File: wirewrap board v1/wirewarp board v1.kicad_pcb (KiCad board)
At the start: 2 copper layers, 99.1 x 99.1 mm, 1369 parts

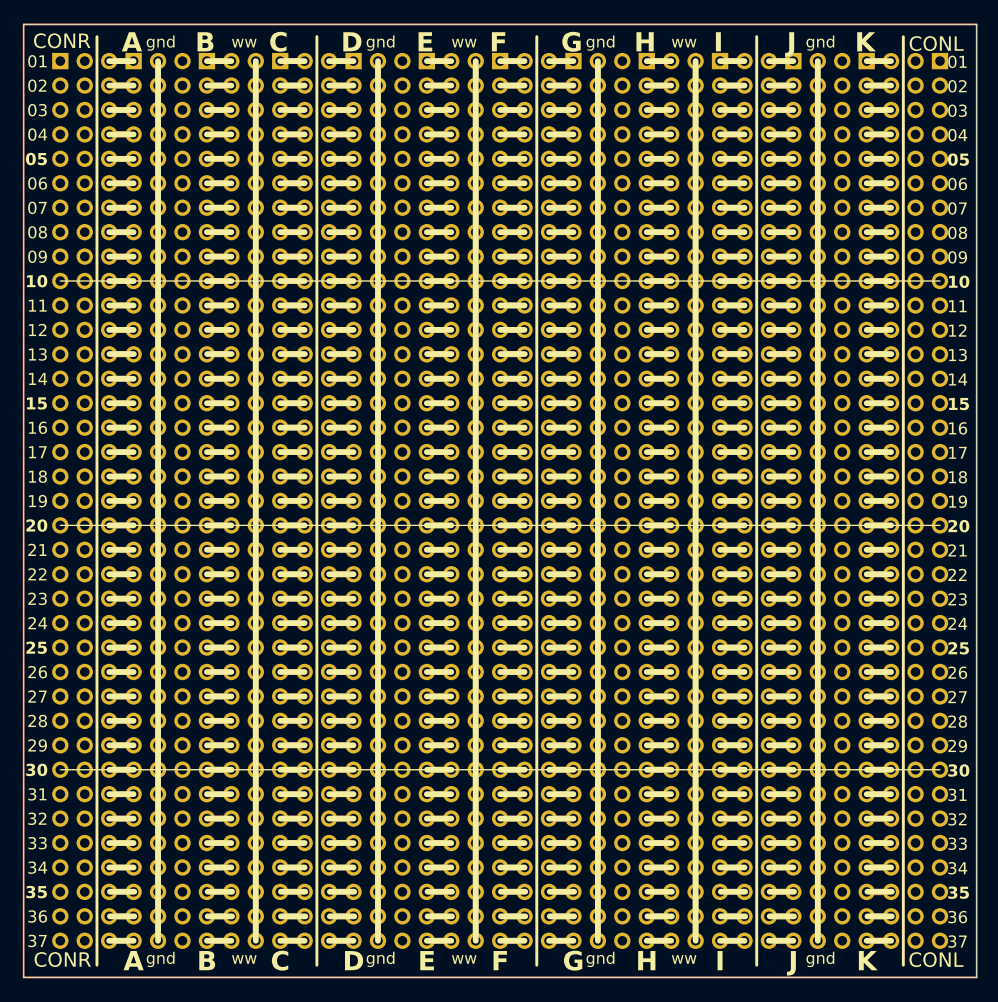
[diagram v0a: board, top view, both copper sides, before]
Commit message: protoboard for wire wrap kicad added v1 v2
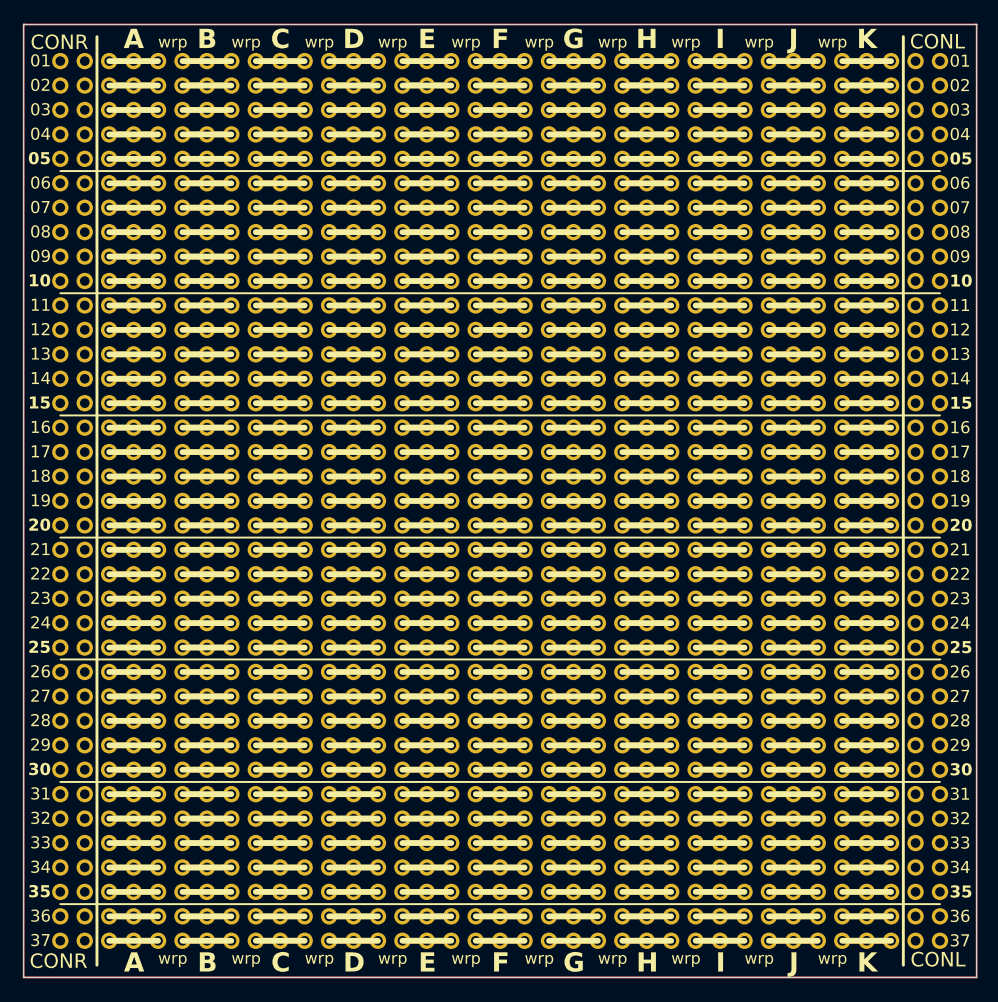
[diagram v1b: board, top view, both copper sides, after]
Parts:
- removed ? (x1369): , 
- added 100: , , F.Cu at (146.1, 82.5)
- added 1000: , , F.Cu at (115.6, 146.1)
- added 1001: , , F.Cu at (115.6, 143.5)
- added 1002: , , F.Cu at (115.6, 141.0)
- added 1003: , , F.Cu at (115.6, 138.4)
- added 1004: , , F.Cu at (115.6, 135.9)
- added 1005: , , F.Cu at (115.6, 133.3)
- added 1006: , , F.Cu at (115.6, 130.8)
- added 1007: , , F.Cu at (115.6, 128.3)
- added 1008: , , F.Cu at (115.6, 125.7)
- added 1009: , , F.Cu at (115.6, 123.2)
- added 101: , , F.Cu at (146.1, 80.0)
- added 1010: , , F.Cu at (115.6, 120.7)
- added 1011: , , F.Cu at (115.6, 118.1)
- added 1012: , , F.Cu at (115.6, 115.6)
- added 1013: , , F.Cu at (115.6, 113.0)
- added 1014: , , F.Cu at (115.6, 110.5)
- added 1015: , , F.Cu at (115.6, 108.0)
- added 1016: , , F.Cu at (115.6, 105.4)
- added 1017: , , F.Cu at (115.6, 102.9)
- added 1018: , , F.Cu at (115.6, 100.3)
- added 1019: , , F.Cu at (115.6, 97.8)
- added 102: , , F.Cu at (146.1, 77.5)
- added 1020: , , F.Cu at (115.6, 95.2)
- added 1021: , , F.Cu at (115.6, 92.7)
- added 1022: , , F.Cu at (115.6, 90.2)
- added 1023: , , F.Cu at (115.6, 87.6)
- added 1024: , , F.Cu at (115.6, 85.1)
- added 1025: , , F.Cu at (115.6, 82.5)
- added 1026: , , F.Cu at (115.6, 80.0)
- added 1027: , , F.Cu at (115.6, 77.5)
- added 1028: , , F.Cu at (115.6, 74.9)
- added 1029: , , F.Cu at (115.6, 72.4)
- added 103: , , F.Cu at (146.1, 74.9)
- added 1030: , , F.Cu at (115.6, 69.8)
- added 1031: , , F.Cu at (115.6, 67.3)
- added 1032: , , F.Cu at (115.6, 64.8)
- added 1033: , , F.Cu at (115.6, 62.2)
- added 1034: , , F.Cu at (115.6, 59.7)
- added 1035: , , F.Cu at (115.6, 57.1)
- added 1036: , , F.Cu at (115.6, 54.6)
- added 1037: , , F.Cu at (118.1, 146.1)
- added 1038: , , F.Cu at (118.1, 143.5)
- added 1039: , , F.Cu at (118.1, 141.0)
- added 104: , , F.Cu at (146.1, 72.4)
- added 1040: , , F.Cu at (118.1, 138.4)
- added 1041: , , F.Cu at (118.1, 135.9)
- added 1042: , , F.Cu at (118.1, 133.3)
- added 1043: , , F.Cu at (118.1, 130.8)
- added 1044: , , F.Cu at (118.1, 128.3)
- added 1045: , , F.Cu at (118.1, 125.7)
- added 1046: , , F.Cu at (118.1, 123.2)
- added 1047: , , F.Cu at (118.1, 120.7)
- added 1048: , , F.Cu at (118.1, 118.1)
- added 1049: , , F.Cu at (118.1, 115.6)
- added 105: , , F.Cu at (146.1, 69.8)
- added 1050: , , F.Cu at (118.1, 113.0)
- added 1051: , , F.Cu at (118.1, 110.5)
- added 1052: , , F.Cu at (118.1, 108.0)
- added 1053: , , F.Cu at (118.1, 105.4)
- added 1054: , , F.Cu at (118.1, 102.9)
- added 1055: , , F.Cu at (118.1, 100.3)
- added 1056: , , F.Cu at (118.1, 97.8)
- added 1057: , , F.Cu at (118.1, 95.2)
- added 1058: , , F.Cu at (118.1, 92.7)
- added 1059: , , F.Cu at (118.1, 90.2)
- added 106: , , F.Cu at (146.1, 67.3)
- added 1060: , , F.Cu at (118.1, 87.6)
- added 1061: , , F.Cu at (118.1, 85.1)
- added 1062: , , F.Cu at (118.1, 82.5)
- added 1063: , , F.Cu at (118.1, 80.0)
- added 1064: , , F.Cu at (118.1, 77.5)
- added 1065: , , F.Cu at (118.1, 74.9)
- added 1066: , , F.Cu at (118.1, 72.4)
- added 1067: , , F.Cu at (118.1, 69.8)
- added 1068: , , F.Cu at (118.1, 67.3)
- added 1069: , , F.Cu at (118.1, 64.8)
- added 107: , , F.Cu at (146.1, 64.8)
- added 1070: , , F.Cu at (118.1, 62.2)
- added 1071: , , F.Cu at (118.1, 59.7)
- added 1072: , , F.Cu at (118.1, 57.1)
- added 1073: , , F.Cu at (118.1, 54.6)
- added 1074: , , F.Cu at (120.7, 146.1)
- added 1075: , , F.Cu at (120.7, 143.5)
- added 1076: , , F.Cu at (120.7, 141.0)
- added 1077: , , F.Cu at (120.7, 138.4)
- added 1078: , , F.Cu at (120.7, 135.9)
- added 1079: , , F.Cu at (120.7, 133.3)
- added 108: , , F.Cu at (146.1, 62.2)
- added 1080: , , F.Cu at (120.7, 130.8)
- added 1081: , , F.Cu at (120.7, 128.3)
- added 1082: , , F.Cu at (120.7, 125.7)
- added 1083: , , F.Cu at (120.7, 123.2)
- added 1084: , , F.Cu at (120.7, 120.7)
- added 1085: , , F.Cu at (120.7, 118.1)
- added 1086: , , F.Cu at (120.7, 115.6)
- added 1087: , , F.Cu at (120.7, 113.0)
- added 1088: , , F.Cu at (120.7, 110.5)
- added 1089: , , F.Cu at (120.7, 108.0)
- added 109: , , F.Cu at (146.1, 59.7)
- added 1090: , , F.Cu at (120.7, 105.4)
- added 1091: , , F.Cu at (120.7, 102.9)
- added 1092: , , F.Cu at (120.7, 100.3)
- added 1093: , , F.Cu at (120.7, 97.8)
- added 1094: , , F.Cu at (120.7, 95.2)
- added 1095: , , F.Cu at (120.7, 92.7)
- added 1096: , , F.Cu at (120.7, 90.2)
- added 1097: , , F.Cu at (120.7, 87.6)
- added 1098: , , F.Cu at (120.7, 85.1)
- added 1099: , , F.Cu at (120.7, 82.5)
- added 110: , , F.Cu at (146.1, 57.1)
- added 1100: , , F.Cu at (120.7, 80.0)
- added 1101: , , F.Cu at (120.7, 77.5)
- added 1102: , , F.Cu at (120.7, 74.9)
- added 1103: , , F.Cu at (120.7, 72.4)
- added 1104: , , F.Cu at (120.7, 69.8)
- added 1105: , , F.Cu at (120.7, 67.3)
- added 1106: , , F.Cu at (120.7, 64.8)
- added 1107: , , F.Cu at (120.7, 62.2)
- added 1108: , , F.Cu at (120.7, 59.7)
- added 1109: , , F.Cu at (120.7, 57.1)
- added 111: , , F.Cu at (146.1, 54.6)
- added 1110: , , F.Cu at (120.7, 54.6)
- added 1111: , , F.Cu at (123.2, 146.1)
- added 1112: , , F.Cu at (123.2, 143.5)
- added 1113: , , F.Cu at (123.2, 141.0)
- added 1114: , , F.Cu at (123.2, 138.4)
- added 1115: , , F.Cu at (123.2, 135.9)
- added 1116: , , F.Cu at (123.2, 133.3)
- added 1117: , , F.Cu at (123.2, 130.8)
- added 1118: , , F.Cu at (123.2, 128.3)
- added 1119: , , F.Cu at (123.2, 125.7)
- added 112: , , F.Cu at (54.6, 146.1)
- added 1120: , , F.Cu at (123.2, 123.2)
- added 1121: , , F.Cu at (123.2, 120.7)
- added 1122: , , F.Cu at (123.2, 118.1)
- added 1123: , , F.Cu at (123.2, 115.6)
- added 1124: , , F.Cu at (123.2, 113.0)
- added 1125: , , F.Cu at (123.2, 110.5)
- added 1126: , , F.Cu at (123.2, 108.0)
- added 1127: , , F.Cu at (123.2, 105.4)
- added 1128: , , F.Cu at (123.2, 102.9)
- added 1129: , , F.Cu at (123.2, 100.3)
- added 113: , , F.Cu at (54.6, 143.5)
- added 1130: , , F.Cu at (123.2, 97.8)
- added 1131: , , F.Cu at (123.2, 95.2)
- added 1132: , , F.Cu at (123.2, 92.7)
- added 1133: , , F.Cu at (123.2, 90.2)
- added 1134: , , F.Cu at (123.2, 87.6)
- added 1135: , , F.Cu at (123.2, 85.1)
- added 1136: , , F.Cu at (123.2, 82.5)
- added 1137: , , F.Cu at (123.2, 80.0)
- added 1138: , , F.Cu at (123.2, 77.5)
- added 1139: , , F.Cu at (123.2, 74.9)
- added 114: , , F.Cu at (54.6, 141.0)
- added 1140: , , F.Cu at (123.2, 72.4)
- added 1141: , , F.Cu at (123.2, 69.8)
- added 1142: , , F.Cu at (123.2, 67.3)
- added 1143: , , F.Cu at (123.2, 64.8)
- added 1144: , , F.Cu at (123.2, 62.2)
- added 1145: , , F.Cu at (123.2, 59.7)
- added 1146: , , F.Cu at (123.2, 57.1)
- added 1147: , , F.Cu at (123.2, 54.6)
- added 1148: , , F.Cu at (125.7, 146.1)
- added 1149: , , F.Cu at (125.7, 143.5)
- added 115: , , F.Cu at (54.6, 138.4)
- added 1150: , , F.Cu at (125.7, 141.0)
- added 1151: , , F.Cu at (125.7, 138.4)
- added 1152: , , F.Cu at (125.7, 135.9)
- added 1153: , , F.Cu at (125.7, 133.3)
- added 1154: , , F.Cu at (125.7, 130.8)
- added 1155: , , F.Cu at (125.7, 128.3)
- added 1156: , , F.Cu at (125.7, 125.7)
- added 1157: , , F.Cu at (125.7, 123.2)
- added 1158: , , F.Cu at (125.7, 120.7)
- added 1159: , , F.Cu at (125.7, 118.1)
- added 116: , , F.Cu at (54.6, 135.9)
- added 1160: , , F.Cu at (125.7, 115.6)
- added 1161: , , F.Cu at (125.7, 113.0)
- added 1162: , , F.Cu at (125.7, 110.5)
- added 1163: , , F.Cu at (125.7, 108.0)
- added 1164: , , F.Cu at (125.7, 105.4)
- added 1165: , , F.Cu at (125.7, 102.9)
- added 1166: , , F.Cu at (125.7, 100.3)
- added 1167: , , F.Cu at (125.7, 97.8)
- added 1168: , , F.Cu at (125.7, 95.2)
- added 1169: , , F.Cu at (125.7, 92.7)
- added 117: , , F.Cu at (54.6, 133.3)
- added 1170: , , F.Cu at (125.7, 90.2)
- added 1171: , , F.Cu at (125.7, 87.6)
- added 1172: , , F.Cu at (125.7, 85.1)
- added 1173: , , F.Cu at (125.7, 82.5)
- added 1174: , , F.Cu at (125.7, 80.0)
- added 1175: , , F.Cu at (125.7, 77.5)
- added 1176: , , F.Cu at (125.7, 74.9)
- added 1177: , , F.Cu at (125.7, 72.4)
- added 1178: , , F.Cu at (125.7, 69.8)
- added 1179: , , F.Cu at (125.7, 67.3)
- added 118: , , F.Cu at (54.6, 130.8)
- added 1180: , , F.Cu at (125.7, 64.8)
- added 1181: , , F.Cu at (125.7, 62.2)
- added 1182: , , F.Cu at (125.7, 59.7)
- added 1183: , , F.Cu at (125.7, 57.1)
- added 1184: , , F.Cu at (125.7, 54.6)
- added 1185: , , F.Cu at (128.3, 146.1)
- added 1186: , , F.Cu at (128.3, 143.5)
- added 1187: , , F.Cu at (128.3, 141.0)
- added 1188: , , F.Cu at (128.3, 138.4)
- added 1189: , , F.Cu at (128.3, 135.9)
- added 119: , , F.Cu at (54.6, 128.3)
- added 1190: , , F.Cu at (128.3, 133.3)
- added 1191: , , F.Cu at (128.3, 130.8)
- added 1192: , , F.Cu at (128.3, 128.3)
- added 1193: , , F.Cu at (128.3, 125.7)
- added 1194: , , F.Cu at (128.3, 123.2)
- added 1195: , , F.Cu at (128.3, 120.7)
- added 1196: , , F.Cu at (128.3, 118.1)
- added 1197: , , F.Cu at (128.3, 115.6)
- added 1198: , , F.Cu at (128.3, 113.0)
- added 1199: , , F.Cu at (128.3, 110.5)
- added 120: , , F.Cu at (54.6, 125.7)
- added 1200: , , F.Cu at (128.3, 108.0)
- added 1201: , , F.Cu at (128.3, 105.4)
- added 1202: , , F.Cu at (128.3, 102.9)
- added 1203: , , F.Cu at (128.3, 100.3)
- added 1204: , , F.Cu at (128.3, 97.8)
- added 1205: , , F.Cu at (128.3, 95.2)
- added 1206: , , F.Cu at (128.3, 92.7)
- added 1207: , , F.Cu at (128.3, 90.2)
- added 1208: , , F.Cu at (128.3, 87.6)
- added 1209: , , F.Cu at (128.3, 85.1)
- added 121: , , F.Cu at (54.6, 123.2)
- added 1210: , , F.Cu at (128.3, 82.5)
- added 1211: , , F.Cu at (128.3, 80.0)
- added 1212: , , F.Cu at (128.3, 77.5)
- added 1213: , , F.Cu at (128.3, 74.9)
- added 1214: , , F.Cu at (128.3, 72.4)
- added 1215: , , F.Cu at (128.3, 69.8)
- added 1216: , , F.Cu at (128.3, 67.3)
- added 1217: , , F.Cu at (128.3, 64.8)
- added 1218: , , F.Cu at (128.3, 62.2)
- added 1219: , , F.Cu at (128.3, 59.7)
- added 122: , , F.Cu at (54.6, 120.7)
- added 1220: , , F.Cu at (128.3, 57.1)
- added 1221: , , F.Cu at (128.3, 54.6)
- added 1222: , , F.Cu at (130.8, 146.1)
- added 1223: , , F.Cu at (130.8, 143.5)
- added 1224: , , F.Cu at (130.8, 141.0)
- added 1225: , , F.Cu at (130.8, 138.4)
- added 1226: , , F.Cu at (130.8, 135.9)
- added 1227: , , F.Cu at (130.8, 133.3)
- added 1228: , , F.Cu at (130.8, 130.8)
- added 1229: , , F.Cu at (130.8, 128.3)
- added 123: , , F.Cu at (54.6, 118.1)
- added 1230: , , F.Cu at (130.8, 125.7)
- added 1231: , , F.Cu at (130.8, 123.2)
- added 1232: , , F.Cu at (130.8, 120.7)
- added 1233: , , F.Cu at (130.8, 118.1)
- added 1234: , , F.Cu at (130.8, 115.6)
- added 1235: , , F.Cu at (130.8, 113.0)
- added 1236: , , F.Cu at (130.8, 110.5)
- added 1237: , , F.Cu at (130.8, 108.0)
- added 1238: , , F.Cu at (130.8, 105.4)
- added 1239: , , F.Cu at (130.8, 102.9)
- added 124: , , F.Cu at (54.6, 115.6)
- added 1240: , , F.Cu at (130.8, 100.3)
- added 1241: , , F.Cu at (130.8, 97.8)
- added 1242: , , F.Cu at (130.8, 95.2)
- added 1243: , , F.Cu at (130.8, 92.7)
- added 1244: , , F.Cu at (130.8, 90.2)
- added 1245: , , F.Cu at (130.8, 87.6)
- added 1246: , , F.Cu at (130.8, 85.1)
- added 1247: , , F.Cu at (130.8, 82.5)
- added 1248: , , F.Cu at (130.8, 80.0)
- added 1249: , , F.Cu at (130.8, 77.5)
- added 125: , , F.Cu at (54.6, 113.0)
- added 1250: , , F.Cu at (130.8, 74.9)
- added 1251: , , F.Cu at (130.8, 72.4)
- added 1252: , , F.Cu at (130.8, 69.8)
- added 1253: , , F.Cu at (130.8, 67.3)
- added 1254: , , F.Cu at (130.8, 64.8)
- added 1255: , , F.Cu at (130.8, 62.2)
- added 1256: , , F.Cu at (130.8, 59.7)
- added 1257: , , F.Cu at (130.8, 57.1)
- added 1258: , , F.Cu at (130.8, 54.6)
- added 1259: , , F.Cu at (133.3, 146.1)
- added 126: , , F.Cu at (54.6, 110.5)
- added 1260: , , F.Cu at (133.3, 143.5)
- added 1261: , , F.Cu at (133.3, 141.0)
- added 1262: , , F.Cu at (133.3, 138.4)
- added 1263: , , F.Cu at (133.3, 135.9)
- added 1264: , , F.Cu at (133.3, 133.3)
- added 1265: , , F.Cu at (133.3, 130.8)
- added 1266: , , F.Cu at (133.3, 128.3)
- added 1267: , , F.Cu at (133.3, 125.7)
- added 1268: , , F.Cu at (133.3, 123.2)
- added 1269: , , F.Cu at (133.3, 120.7)
- added 127: , , F.Cu at (54.6, 108.0)
- added 1270: , , F.Cu at (133.3, 118.1)
- added 1271: , , F.Cu at (133.3, 115.6)
- added 1272: , , F.Cu at (133.3, 113.0)
- added 1273: , , F.Cu at (133.3, 110.5)
- added 1274: , , F.Cu at (133.3, 108.0)
- added 1275: , , F.Cu at (133.3, 105.4)
- added 1276: , , F.Cu at (133.3, 102.9)
- added 1277: , , F.Cu at (133.3, 100.3)
- added 1278: , , F.Cu at (133.3, 97.8)
- added 1279: , , F.Cu at (133.3, 95.2)
- added 128: , , F.Cu at (54.6, 105.4)
- added 1280: , , F.Cu at (133.3, 92.7)
- added 1281: , , F.Cu at (133.3, 90.2)
- added 1282: , , F.Cu at (133.3, 87.6)
- added 1283: , , F.Cu at (133.3, 85.1)
- added 1284: , , F.Cu at (133.3, 82.5)
- added 1285: , , F.Cu at (133.3, 80.0)
- added 1286: , , F.Cu at (133.3, 77.5)
- added 1287: , , F.Cu at (133.3, 74.9)
- added 1288: , , F.Cu at (133.3, 72.4)
- added 1289: , , F.Cu at (133.3, 69.8)
- added 129: , , F.Cu at (54.6, 102.9)
- added 1290: , , F.Cu at (133.3, 67.3)
- added 1291: , , F.Cu at (133.3, 64.8)
- added 1292: , , F.Cu at (133.3, 62.2)
- added 1293: , , F.Cu at (133.3, 59.7)
- added 1294: , , F.Cu at (133.3, 57.1)
- added 1295: , , F.Cu at (133.3, 54.6)
- added 1296: , , F.Cu at (135.9, 146.1)
- added 1297: , , F.Cu at (135.9, 143.5)
- added 1298: , , F.Cu at (135.9, 141.0)
- added 1299: , , F.Cu at (135.9, 138.4)
- added 130: , , F.Cu at (54.6, 100.3)
- added 1300: , , F.Cu at (135.9, 135.9)
- added 1301: , , F.Cu at (135.9, 133.3)
- added 1302: , , F.Cu at (135.9, 130.8)
- added 1303: , , F.Cu at (135.9, 128.3)
- added 1304: , , F.Cu at (135.9, 125.7)
- added 1305: , , F.Cu at (135.9, 123.2)
- added 1306: , , F.Cu at (135.9, 120.7)
- added 1307: , , F.Cu at (135.9, 118.1)
- added 1308: , , F.Cu at (135.9, 115.6)
- added 1309: , , F.Cu at (135.9, 113.0)
- added 131: , , F.Cu at (54.6, 97.8)
- added 1310: , , F.Cu at (135.9, 110.5)
- added 1311: , , F.Cu at (135.9, 108.0)
- added 1312: , , F.Cu at (135.9, 105.4)
- added 1313: , , F.Cu at (135.9, 102.9)
- added 1314: , , F.Cu at (135.9, 100.3)
- added 1315: , , F.Cu at (135.9, 97.8)
- added 1316: , , F.Cu at (135.9, 95.2)
- added 1317: , , F.Cu at (135.9, 92.7)
- added 1318: , , F.Cu at (135.9, 90.2)
- added 1319: , , F.Cu at (135.9, 87.6)
- added 132: , , F.Cu at (54.6, 95.2)
- added 1320: , , F.Cu at (135.9, 85.1)
- added 1321: , , F.Cu at (135.9, 82.5)
- added 1322: , , F.Cu at (135.9, 80.0)
- added 1323: , , F.Cu at (135.9, 77.5)
- added 1324: , , F.Cu at (135.9, 74.9)
- added 1325: , , F.Cu at (135.9, 72.4)
- added 1326: , , F.Cu at (135.9, 69.8)
- added 1327: , , F.Cu at (135.9, 67.3)
- added 1328: , , F.Cu at (135.9, 64.8)
- added 1329: , , F.Cu at (135.9, 62.2)
- added 133: , , F.Cu at (54.6, 92.7)
- added 1330: , , F.Cu at (135.9, 59.7)
- added 1331: , , F.Cu at (135.9, 57.1)
- added 1332: , , F.Cu at (135.9, 54.6)
- added 1333: , , F.Cu at (138.4, 146.1)
- added 1334: , , F.Cu at (138.4, 143.5)
- added 1335: , , F.Cu at (138.4, 141.0)
- added 1336: , , F.Cu at (138.4, 138.4)
- added 1337: , , F.Cu at (138.4, 135.9)
- added 1338: , , F.Cu at (138.4, 133.3)
- added 1339: , , F.Cu at (138.4, 130.8)
- added 134: , , F.Cu at (54.6, 90.2)
- added 1340: , , F.Cu at (138.4, 128.3)
- added 1341: , , F.Cu at (138.4, 125.7)
- added 1342: , , F.Cu at (138.4, 123.2)
- added 1343: , , F.Cu at (138.4, 120.7)
- added 1344: , , F.Cu at (138.4, 118.1)
- added 1345: , , F.Cu at (138.4, 115.6)
- added 1346: , , F.Cu at (138.4, 113.0)
- added 1347: , , F.Cu at (138.4, 110.5)
- added 1348: , , F.Cu at (138.4, 108.0)
- added 1349: , , F.Cu at (138.4, 105.4)
- added 135: , , F.Cu at (54.6, 87.6)
- added 1350: , , F.Cu at (138.4, 102.9)
- added 1351: , , F.Cu at (138.4, 100.3)
- added 1352: , , F.Cu at (138.4, 97.8)
- added 1353: , , F.Cu at (138.4, 95.2)
- added 1354: , , F.Cu at (138.4, 92.7)
- added 1355: , , F.Cu at (138.4, 90.2)
- added 1356: , , F.Cu at (138.4, 87.6)
- added 1357: , , F.Cu at (138.4, 85.1)
- added 1358: , , F.Cu at (138.4, 82.5)
- added 1359: , , F.Cu at (138.4, 80.0)
- added 136: , , F.Cu at (54.6, 85.1)
- added 1360: , , F.Cu at (138.4, 77.5)
- added 1361: , , F.Cu at (138.4, 74.9)
- added 1362: , , F.Cu at (138.4, 72.4)
- added 1363: , , F.Cu at (138.4, 69.8)
- added 1364: , , F.Cu at (138.4, 67.3)
- added 1365: , , F.Cu at (138.4, 64.8)
- added 1366: , , F.Cu at (138.4, 62.2)
- added 1367: , , F.Cu at (138.4, 59.7)
- added 1368: , , F.Cu at (138.4, 57.1)
- added 1369: , , F.Cu at (138.4, 54.6)
- added 137: , , F.Cu at (54.6, 82.5)
- added 1370: , , F.Cu at (141.0, 146.1)
- added 1371: , , F.Cu at (141.0, 143.5)
- added 1372: , , F.Cu at (141.0, 141.0)
- added 1373: , , F.Cu at (141.0, 138.4)
- added 1374: , , F.Cu at (141.0, 135.9)
- added 1375: , , F.Cu at (141.0, 133.3)
- added 1376: , , F.Cu at (141.0, 130.8)
- added 1377: , , F.Cu at (141.0, 128.3)
- added 1378: , , F.Cu at (141.0, 125.7)
- added 1379: , , F.Cu at (141.0, 123.2)
- added 138: , , F.Cu at (54.6, 80.0)
- added 1380: , , F.Cu at (141.0, 120.7)
- added 1381: , , F.Cu at (141.0, 118.1)
- added 1382: , , F.Cu at (141.0, 115.6)
- added 1383: , , F.Cu at (141.0, 113.0)
- added 1384: , , F.Cu at (141.0, 110.5)
- added 1385: , , F.Cu at (141.0, 108.0)
- added 1386: , , F.Cu at (141.0, 105.4)
- added 1387: , , F.Cu at (141.0, 102.9)
- added 1388: , , F.Cu at (141.0, 100.3)
- added 1389: , , F.Cu at (141.0, 97.8)
- added 139: , , F.Cu at (54.6, 77.5)
- added 1390: , , F.Cu at (141.0, 95.2)
- added 1391: , , F.Cu at (141.0, 92.7)
- added 1392: , , F.Cu at (141.0, 90.2)
- added 1393: , , F.Cu at (141.0, 87.6)
- added 1394: , , F.Cu at (141.0, 85.1)
- added 1395: , , F.Cu at (141.0, 82.5)
- added 1396: , , F.Cu at (141.0, 80.0)
- added 1397: , , F.Cu at (141.0, 77.5)
- added 1398: , , F.Cu at (141.0, 74.9)
- added 1399: , , F.Cu at (141.0, 72.4)
- added 140: , , F.Cu at (54.6, 74.9)
- added 1400: , , F.Cu at (141.0, 69.8)
- added 1401: , , F.Cu at (141.0, 67.3)
- added 1402: , , F.Cu at (141.0, 64.8)
- added 1403: , , F.Cu at (141.0, 62.2)
- added 1404: , , F.Cu at (141.0, 59.7)
- added 1405: , , F.Cu at (141.0, 57.1)
- added 1406: , , F.Cu at (141.0, 54.6)
- added 1407: , , F.Cu at (143.5, 146.1)
- added 1408: , , F.Cu at (143.5, 143.5)
- added 1409: , , F.Cu at (143.5, 141.0)
- added 141: , , F.Cu at (54.6, 72.4)
- added 1410: , , F.Cu at (143.5, 138.4)
- added 1411: , , F.Cu at (143.5, 135.9)
- added 1412: , , F.Cu at (143.5, 133.3)
- added 1413: , , F.Cu at (143.5, 130.8)
- added 1414: , , F.Cu at (143.5, 128.3)
- added 1415: , , F.Cu at (143.5, 125.7)
- added 1416: , , F.Cu at (143.5, 123.2)
- added 1417: , , F.Cu at (143.5, 120.7)
- added 1418: , , F.Cu at (143.5, 118.1)
- added 1419: , , F.Cu at (143.5, 115.6)
- added 142: , , F.Cu at (54.6, 69.8)
- added 1420: , , F.Cu at (143.5, 113.0)
- added 1421: , , F.Cu at (143.5, 110.5)
- added 1422: , , F.Cu at (143.5, 108.0)
- added 1423: , , F.Cu at (143.5, 105.4)
- added 1424: , , F.Cu at (143.5, 102.9)
- added 1425: , , F.Cu at (143.5, 100.3)
- added 1426: , , F.Cu at (143.5, 97.8)
- added 1427: , , F.Cu at (143.5, 95.2)
- added 1428: , , F.Cu at (143.5, 92.7)
- added 1429: , , F.Cu at (143.5, 90.2)
- added 143: , , F.Cu at (54.6, 67.3)
- added 1430: , , F.Cu at (143.5, 87.6)
- added 1431: , , F.Cu at (143.5, 85.1)
- added 1432: , , F.Cu at (143.5, 82.5)
- added 1433: , , F.Cu at (143.5, 80.0)
- added 1434: , , F.Cu at (143.5, 77.5)
- added 1435: , , F.Cu at (143.5, 74.9)
- added 1436: , , F.Cu at (143.5, 72.4)
- added 1437: , , F.Cu at (143.5, 69.8)
- added 1438: , , F.Cu at (143.5, 67.3)
- added 1439: , , F.Cu at (143.5, 64.8)
- added 144: , , F.Cu at (54.6, 64.8)
- added 1440: , , F.Cu at (143.5, 62.2)
- added 1441: , , F.Cu at (143.5, 59.7)
- added 1442: , , F.Cu at (143.5, 57.1)
- added 1443: , , F.Cu at (143.5, 54.6)
- added 145: , , F.Cu at (54.6, 62.2)
- added 146: , , F.Cu at (54.6, 59.7)
- added 147: , , F.Cu at (54.6, 57.1)
- added 148: , , F.Cu at (54.6, 54.6)
- added 149: , , F.Cu at (57.1, 146.1)
- added 150: , , F.Cu at (57.1, 143.5)
- added 151: , , F.Cu at (57.1, 141.0)
- added 152: , , F.Cu at (57.1, 138.4)
- added 153: , , F.Cu at (57.1, 135.9)
- added 154: , , F.Cu at (57.1, 133.3)
- added 155: , , F.Cu at (57.1, 130.8)
- added 156: , , F.Cu at (57.1, 128.3)
- added 157: , , F.Cu at (57.1, 125.7)
- added 158: , , F.Cu at (57.1, 123.2)
- added 159: , , F.Cu at (57.1, 120.7)
- added 160: , , F.Cu at (57.1, 118.1)
- added 161: , , F.Cu at (57.1, 115.6)
- added 162: , , F.Cu at (57.1, 113.0)
- added 163: , , F.Cu at (57.1, 110.5)
- added 164: , , F.Cu at (57.1, 108.0)
- added 165: , , F.Cu at (57.1, 105.4)
- added 166: , , F.Cu at (57.1, 102.9)
- added 167: , , F.Cu at (57.1, 100.3)
- added 168: , , F.Cu at (57.1, 97.8)
- added 169: , , F.Cu at (57.1, 95.2)
- added 170: , , F.Cu at (57.1, 92.7)
- added 171: , , F.Cu at (57.1, 90.2)
- added 172: , , F.Cu at (57.1, 87.6)
- added 173: , , F.Cu at (57.1, 85.1)
- added 174: , , F.Cu at (57.1, 82.5)
- added 175: , , F.Cu at (57.1, 80.0)
- added 176: , , F.Cu at (57.1, 77.5)
- added 177: , , F.Cu at (57.1, 74.9)
- added 178: , , F.Cu at (57.1, 72.4)
- added 179: , , F.Cu at (57.1, 69.8)
- added 180: , , F.Cu at (57.1, 67.3)
- added 181: , , F.Cu at (57.1, 64.8)
- added 182: , , F.Cu at (57.1, 62.2)
- added 183: , , F.Cu at (57.1, 59.7)
- added 184: , , F.Cu at (57.1, 57.1)
- added 185: , , F.Cu at (57.1, 54.6)
- added 186: , , F.Cu at (59.7, 146.1)
- added 187: , , F.Cu at (59.7, 143.5)
- added 188: , , F.Cu at (59.7, 141.0)
- added 189: , , F.Cu at (59.7, 138.4)
- added 190: , , F.Cu at (59.7, 135.9)
- added 191: , , F.Cu at (59.7, 133.3)
- added 192: , , F.Cu at (59.7, 130.8)
- added 193: , , F.Cu at (59.7, 128.3)
- added 194: , , F.Cu at (59.7, 125.7)
- added 195: , , F.Cu at (59.7, 123.2)
- added 196: , , F.Cu at (59.7, 120.7)
- added 197: , , F.Cu at (59.7, 118.1)
- added 198: , , F.Cu at (59.7, 115.6)
- added 199: , , F.Cu at (59.7, 113.0)
- added 200: , , F.Cu at (59.7, 110.5)
- added 201: , , F.Cu at (59.7, 108.0)
- added 202: , , F.Cu at (59.7, 105.4)
- added 203: , , F.Cu at (59.7, 102.9)
- added 204: , , F.Cu at (59.7, 100.3)
- added 205: , , F.Cu at (59.7, 97.8)
- added 206: , , F.Cu at (59.7, 95.2)
- added 207: , , F.Cu at (59.7, 92.7)
- added 208: , , F.Cu at (59.7, 90.2)
- added 209: , , F.Cu at (59.7, 87.6)
- added 210: , , F.Cu at (59.7, 85.1)
- added 211: , , F.Cu at (59.7, 82.5)
- added 212: , , F.Cu at (59.7, 80.0)
- added 213: , , F.Cu at (59.7, 77.5)
- added 214: , , F.Cu at (59.7, 74.9)
- added 215: , , F.Cu at (59.7, 72.4)
- added 216: , , F.Cu at (59.7, 69.8)
- added 217: , , F.Cu at (59.7, 67.3)
- added 218: , , F.Cu at (59.7, 64.8)
- added 219: , , F.Cu at (59.7, 62.2)
- added 220: , , F.Cu at (59.7, 59.7)
- added 221: , , F.Cu at (59.7, 57.1)
- added 222: , , F.Cu at (59.7, 54.6)
- added 223: , , F.Cu at (62.2, 146.1)
- added 224: , , F.Cu at (62.2, 143.5)
- added 225: , , F.Cu at (62.2, 141.0)
- added 226: , , F.Cu at (62.2, 138.4)
- added 227: , , F.Cu at (62.2, 135.9)
- added 228: , , F.Cu at (62.2, 133.3)
- added 229: , , F.Cu at (62.2, 130.8)
- added 230: , , F.Cu at (62.2, 128.3)
- added 231: , , F.Cu at (62.2, 125.7)
- added 232: , , F.Cu at (62.2, 123.2)
- added 233: , , F.Cu at (62.2, 120.7)
- added 234: , , F.Cu at (62.2, 118.1)
- added 235: , , F.Cu at (62.2, 115.6)
- added 236: , , F.Cu at (62.2, 113.0)
- added 237: , , F.Cu at (62.2, 110.5)
- added 238: , , F.Cu at (62.2, 108.0)
- added 239: , , F.Cu at (62.2, 105.4)
- added 240: , , F.Cu at (62.2, 102.9)
- added 241: , , F.Cu at (62.2, 100.3)
- added 242: , , F.Cu at (62.2, 97.8)
- added 243: , , F.Cu at (62.2, 95.2)
- added 244: , , F.Cu at (62.2, 92.7)
- added 245: , , F.Cu at (62.2, 90.2)
- added 246: , , F.Cu at (62.2, 87.6)
- added 247: , , F.Cu at (62.2, 85.1)
- added 248: , , F.Cu at (62.2, 82.5)
- added 249: , , F.Cu at (62.2, 80.0)
- added 250: , , F.Cu at (62.2, 77.5)
- added 251: , , F.Cu at (62.2, 74.9)
- added 252: , , F.Cu at (62.2, 72.4)
- added 253: , , F.Cu at (62.2, 69.8)
- added 254: , , F.Cu at (62.2, 67.3)
- added 255: , , F.Cu at (62.2, 64.8)
- added 256: , , F.Cu at (62.2, 62.2)
- added 257: , , F.Cu at (62.2, 59.7)
- added 258: , , F.Cu at (62.2, 57.1)
- added 259: , , F.Cu at (62.2, 54.6)
- added 260: , , F.Cu at (64.8, 146.1)
- added 261: , , F.Cu at (64.8, 143.5)
- added 262: , , F.Cu at (64.8, 141.0)
- added 263: , , F.Cu at (64.8, 138.4)
- added 264: , , F.Cu at (64.8, 135.9)
- added 265: , , F.Cu at (64.8, 133.3)
- added 266: , , F.Cu at (64.8, 130.8)
- added 267: , , F.Cu at (64.8, 128.3)
- added 268: , , F.Cu at (64.8, 125.7)
- added 269: , , F.Cu at (64.8, 123.2)
- added 270: , , F.Cu at (64.8, 120.7)
- added 271: , , F.Cu at (64.8, 118.1)
- added 272: , , F.Cu at (64.8, 115.6)
- added 273: , , F.Cu at (64.8, 113.0)
- added 274: , , F.Cu at (64.8, 110.5)
- added 275: , , F.Cu at (64.8, 108.0)
- added 276: , , F.Cu at (64.8, 105.4)
- added 277: , , F.Cu at (64.8, 102.9)
- added 278: , , F.Cu at (64.8, 100.3)
- added 279: , , F.Cu at (64.8, 97.8)
- added 280: , , F.Cu at (64.8, 95.2)
- added 281: , , F.Cu at (64.8, 92.7)
- added 282: , , F.Cu at (64.8, 90.2)
- added 283: , , F.Cu at (64.8, 87.6)
- added 284: , , F.Cu at (64.8, 85.1)
- added 285: , , F.Cu at (64.8, 82.5)
- added 286: , , F.Cu at (64.8, 80.0)
- added 287: , , F.Cu at (64.8, 77.5)
- added 288: , , F.Cu at (64.8, 74.9)
- added 289: , , F.Cu at (64.8, 72.4)
- added 290: , , F.Cu at (64.8, 69.8)
- added 291: , , F.Cu at (64.8, 67.3)
- added 292: , , F.Cu at (64.8, 64.8)
- added 293: , , F.Cu at (64.8, 62.2)
- added 294: , , F.Cu at (64.8, 59.7)
- added 295: , , F.Cu at (64.8, 57.1)
- added 296: , , F.Cu at (64.8, 54.6)
- added 297: , , F.Cu at (67.3, 146.1)
- added 298: , , F.Cu at (67.3, 143.5)
- added 299: , , F.Cu at (67.3, 141.0)
- added 300: , , F.Cu at (67.3, 138.4)
- added 301: , , F.Cu at (67.3, 135.9)
- added 302: , , F.Cu at (67.3, 133.3)
- added 303: , , F.Cu at (67.3, 130.8)
- added 304: , , F.Cu at (67.3, 128.3)
- added 305: , , F.Cu at (67.3, 125.7)
- added 306: , , F.Cu at (67.3, 123.2)
- added 307: , , F.Cu at (67.3, 120.7)
- added 308: , , F.Cu at (67.3, 118.1)
- added 309: , , F.Cu at (67.3, 115.6)
- added 310: , , F.Cu at (67.3, 113.0)
- added 311: , , F.Cu at (67.3, 110.5)
- added 312: , , F.Cu at (67.3, 108.0)
- added 313: , , F.Cu at (67.3, 105.4)
- added 314: , , F.Cu at (67.3, 102.9)
- added 315: , , F.Cu at (67.3, 100.3)
- added 316: , , F.Cu at (67.3, 97.8)
- added 317: , , F.Cu at (67.3, 95.2)
- added 318: , , F.Cu at (67.3, 92.7)
- added 319: , , F.Cu at (67.3, 90.2)
- added 320: , , F.Cu at (67.3, 87.6)
- added 321: , , F.Cu at (67.3, 85.1)
- added 322: , , F.Cu at (67.3, 82.5)
- added 323: , , F.Cu at (67.3, 80.0)
- added 324: , , F.Cu at (67.3, 77.5)
- added 325: , , F.Cu at (67.3, 74.9)
- added 326: , , F.Cu at (67.3, 72.4)
- added 327: , , F.Cu at (67.3, 69.8)
- added 328: , , F.Cu at (67.3, 67.3)
- added 329: , , F.Cu at (67.3, 64.8)
- added 330: , , F.Cu at (67.3, 62.2)
- added 331: , , F.Cu at (67.3, 59.7)
- added 332: , , F.Cu at (67.3, 57.1)
- added 333: , , F.Cu at (67.3, 54.6)
- added 334: , , F.Cu at (69.8, 146.1)
- added 335: , , F.Cu at (69.8, 143.5)
- added 336: , , F.Cu at (69.8, 141.0)
- added 337: , , F.Cu at (69.8, 138.4)
- added 338: , , F.Cu at (69.8, 135.9)
- added 339: , , F.Cu at (69.8, 133.3)
- added 340: , , F.Cu at (69.8, 130.8)
- added 341: , , F.Cu at (69.8, 128.3)
- added 342: , , F.Cu at (69.8, 125.7)
- added 343: , , F.Cu at (69.8, 123.2)
- added 344: , , F.Cu at (69.8, 120.7)
- added 345: , , F.Cu at (69.8, 118.1)
- added 346: , , F.Cu at (69.8, 115.6)
- added 347: , , F.Cu at (69.8, 113.0)
- added 348: , , F.Cu at (69.8, 110.5)
- added 349: , , F.Cu at (69.8, 108.0)
- added 350: , , F.Cu at (69.8, 105.4)
- added 351: , , F.Cu at (69.8, 102.9)
- added 352: , , F.Cu at (69.8, 100.3)
- added 353: , , F.Cu at (69.8, 97.8)
- added 354: , , F.Cu at (69.8, 95.2)
- added 355: , , F.Cu at (69.8, 92.7)
- added 356: , , F.Cu at (69.8, 90.2)
- added 357: , , F.Cu at (69.8, 87.6)
- added 358: , , F.Cu at (69.8, 85.1)
- added 359: , , F.Cu at (69.8, 82.5)
- added 360: , , F.Cu at (69.8, 80.0)
- added 361: , , F.Cu at (69.8, 77.5)
- added 362: , , F.Cu at (69.8, 74.9)
- added 363: , , F.Cu at (69.8, 72.4)
- added 364: , , F.Cu at (69.8, 69.8)
- added 365: , , F.Cu at (69.8, 67.3)
- added 366: , , F.Cu at (69.8, 64.8)
- added 367: , , F.Cu at (69.8, 62.2)
- added 368: , , F.Cu at (69.8, 59.7)
- added 369: , , F.Cu at (69.8, 57.1)
- added 370: , , F.Cu at (69.8, 54.6)
- added 371: , , F.Cu at (72.4, 146.1)
- added 372: , , F.Cu at (72.4, 143.5)
- added 373: , , F.Cu at (72.4, 141.0)
- added 374: , , F.Cu at (72.4, 138.4)
- added 375: , , F.Cu at (72.4, 135.9)
- added 376: , , F.Cu at (72.4, 133.3)
- added 377: , , F.Cu at (72.4, 130.8)
- added 378: , , F.Cu at (72.4, 128.3)
- added 379: , , F.Cu at (72.4, 125.7)
- added 380: , , F.Cu at (72.4, 123.2)
- added 381: , , F.Cu at (72.4, 120.7)
- added 382: , , F.Cu at (72.4, 118.1)
- added 383: , , F.Cu at (72.4, 115.6)
- added 384: , , F.Cu at (72.4, 113.0)
- added 385: , , F.Cu at (72.4, 110.5)
- added 386: , , F.Cu at (72.4, 108.0)
- added 387: , , F.Cu at (72.4, 105.4)
- added 388: , , F.Cu at (72.4, 102.9)
- added 389: , , F.Cu at (72.4, 100.3)
- added 390: , , F.Cu at (72.4, 97.8)
- added 391: , , F.Cu at (72.4, 95.2)
- added 392: , , F.Cu at (72.4, 92.7)
- added 393: , , F.Cu at (72.4, 90.2)
- added 394: , , F.Cu at (72.4, 87.6)
- added 395: , , F.Cu at (72.4, 85.1)
- added 396: , , F.Cu at (72.4, 82.5)
- added 397: , , F.Cu at (72.4, 80.0)
- added 398: , , F.Cu at (72.4, 77.5)
- added 399: , , F.Cu at (72.4, 74.9)
- added 400: , , F.Cu at (72.4, 72.4)
- added 401: , , F.Cu at (72.4, 69.8)
- added 402: , , F.Cu at (72.4, 67.3)
- added 403: , , F.Cu at (72.4, 64.8)
- added 404: , , F.Cu at (72.4, 62.2)
- added 405: , , F.Cu at (72.4, 59.7)
- added 406: , , F.Cu at (72.4, 57.1)
- added 407: , , F.Cu at (72.4, 54.6)
- added 408: , , F.Cu at (74.9, 146.1)
- added 409: , , F.Cu at (74.9, 143.5)
- added 410: , , F.Cu at (74.9, 141.0)
- added 411: , , F.Cu at (74.9, 138.4)
- added 412: , , F.Cu at (74.9, 135.9)
- added 413: , , F.Cu at (74.9, 133.3)
- added 414: , , F.Cu at (74.9, 130.8)
- added 415: , , F.Cu at (74.9, 128.3)
- added 416: , , F.Cu at (74.9, 125.7)
- added 417: , , F.Cu at (74.9, 123.2)
- added 418: , , F.Cu at (74.9, 120.7)
- added 419: , , F.Cu at (74.9, 118.1)
- added 420: , , F.Cu at (74.9, 115.6)
- added 421: , , F.Cu at (74.9, 113.0)
- added 422: , , F.Cu at (74.9, 110.5)
- added 423: , , F.Cu at (74.9, 108.0)
- added 424: , , F.Cu at (74.9, 105.4)
- added 425: , , F.Cu at (74.9, 102.9)
- added 426: , , F.Cu at (74.9, 100.3)
- added 427: , , F.Cu at (74.9, 97.8)
- added 428: , , F.Cu at (74.9, 95.2)
- added 429: , , F.Cu at (74.9, 92.7)
- added 430: , , F.Cu at (74.9, 90.2)
- added 431: , , F.Cu at (74.9, 87.6)
- added 432: , , F.Cu at (74.9, 85.1)
- added 433: , , F.Cu at (74.9, 82.5)
- added 434: , , F.Cu at (74.9, 80.0)
- added 435: , , F.Cu at (74.9, 77.5)
- added 436: , , F.Cu at (74.9, 74.9)
- added 437: , , F.Cu at (74.9, 72.4)
- added 438: , , F.Cu at (74.9, 69.8)
- added 439: , , F.Cu at (74.9, 67.3)
- added 440: , , F.Cu at (74.9, 64.8)
- added 441: , , F.Cu at (74.9, 62.2)
- added 442: , , F.Cu at (74.9, 59.7)
- added 443: , , F.Cu at (74.9, 57.1)
- added 444: , , F.Cu at (74.9, 54.6)
- added 445: , , F.Cu at (77.5, 146.1)
- added 446: , , F.Cu at (77.5, 143.5)
- added 447: , , F.Cu at (77.5, 141.0)
- added 448: , , F.Cu at (77.5, 138.4)
- added 449: , , F.Cu at (77.5, 135.9)
- added 450: , , F.Cu at (77.5, 133.3)
- added 451: , , F.Cu at (77.5, 130.8)
- added 452: , , F.Cu at (77.5, 128.3)
- added 453: , , F.Cu at (77.5, 125.7)
- added 454: , , F.Cu at (77.5, 123.2)
- added 455: , , F.Cu at (77.5, 120.7)
- added 456: , , F.Cu at (77.5, 118.1)
- added 457: , , F.Cu at (77.5, 115.6)
- added 458: , , F.Cu at (77.5, 113.0)
- added 459: , , F.Cu at (77.5, 110.5)
- added 460: , , F.Cu at (77.5, 108.0)
- added 461: , , F.Cu at (77.5, 105.4)
- added 462: , , F.Cu at (77.5, 102.9)
- added 463: , , F.Cu at (77.5, 100.3)
- added 464: , , F.Cu at (77.5, 97.8)
- added 465: , , F.Cu at (77.5, 95.2)
- added 466: , , F.Cu at (77.5, 92.7)
- added 467: , , F.Cu at (77.5, 90.2)
- added 468: , , F.Cu at (77.5, 87.6)
- added 469: , , F.Cu at (77.5, 85.1)
- added 470: , , F.Cu at (77.5, 82.5)
- added 471: , , F.Cu at (77.5, 80.0)
- added 472: , , F.Cu at (77.5, 77.5)
- added 473: , , F.Cu at (77.5, 74.9)
- added 474: , , F.Cu at (77.5, 72.4)
- added 475: , , F.Cu at (77.5, 69.8)
- added 476: , , F.Cu at (77.5, 67.3)
- added 477: , , F.Cu at (77.5, 64.8)
- added 478: , , F.Cu at (77.5, 62.2)
- added 479: , , F.Cu at (77.5, 59.7)
- added 480: , , F.Cu at (77.5, 57.1)
- added 481: , , F.Cu at (77.5, 54.6)
- added 482: , , F.Cu at (80.0, 146.1)
- added 483: , , F.Cu at (80.0, 143.5)
- added 484: , , F.Cu at (80.0, 141.0)
- added 485: , , F.Cu at (80.0, 138.4)
- added 486: , , F.Cu at (80.0, 135.9)
- added 487: , , F.Cu at (80.0, 133.3)
- added 488: , , F.Cu at (80.0, 130.8)
- added 489: , , F.Cu at (80.0, 128.3)
- added 490: , , F.Cu at (80.0, 125.7)
- added 491: , , F.Cu at (80.0, 123.2)
- added 492: , , F.Cu at (80.0, 120.7)
- added 493: , , F.Cu at (80.0, 118.1)
- added 494: , , F.Cu at (80.0, 115.6)
- added 495: , , F.Cu at (80.0, 113.0)
- added 496: , , F.Cu at (80.0, 110.5)
- added 497: , , F.Cu at (80.0, 108.0)
- added 498: , , F.Cu at (80.0, 105.4)
- added 499: , , F.Cu at (80.0, 102.9)
- added 500: , , F.Cu at (80.0, 100.3)
- added 501: , , F.Cu at (80.0, 97.8)
- added 502: , , F.Cu at (80.0, 95.2)
- added 503: , , F.Cu at (80.0, 92.7)
- added 504: , , F.Cu at (80.0, 90.2)
- added 505: , , F.Cu at (80.0, 87.6)
- added 506: , , F.Cu at (80.0, 85.1)
- added 507: , , F.Cu at (80.0, 82.5)
- added 508: , , F.Cu at (80.0, 80.0)
- added 509: , , F.Cu at (80.0, 77.5)
- added 510: , , F.Cu at (80.0, 74.9)
- added 511: , , F.Cu at (80.0, 72.4)
- added 512: , , F.Cu at (80.0, 69.8)
- added 513: , , F.Cu at (80.0, 67.3)
- added 514: , , F.Cu at (80.0, 64.8)
- added 515: , , F.Cu at (80.0, 62.2)
- added 516: , , F.Cu at (80.0, 59.7)
- added 517: , , F.Cu at (80.0, 57.1)
- added 518: , , F.Cu at (80.0, 54.6)
- added 519: , , F.Cu at (82.5, 146.1)
- added 520: , , F.Cu at (82.5, 143.5)
- added 521: , , F.Cu at (82.5, 141.0)
- added 522: , , F.Cu at (82.5, 138.4)
- added 523: , , F.Cu at (82.5, 135.9)
- added 524: , , F.Cu at (82.5, 133.3)
- added 525: , , F.Cu at (82.5, 130.8)
- added 526: , , F.Cu at (82.5, 128.3)
- added 527: , , F.Cu at (82.5, 125.7)
- added 528: , , F.Cu at (82.5, 123.2)
- added 529: , , F.Cu at (82.5, 120.7)
- added 530: , , F.Cu at (82.5, 118.1)
- added 531: , , F.Cu at (82.5, 115.6)
- added 532: , , F.Cu at (82.5, 113.0)
- added 533: , , F.Cu at (82.5, 110.5)
- added 534: , , F.Cu at (82.5, 108.0)
- added 535: , , F.Cu at (82.5, 105.4)
- added 536: , , F.Cu at (82.5, 102.9)
- added 537: , , F.Cu at (82.5, 100.3)
- added 538: , , F.Cu at (82.5, 97.8)
- added 539: , , F.Cu at (82.5, 95.2)
- added 540: , , F.Cu at (82.5, 92.7)
- added 541: , , F.Cu at (82.5, 90.2)
- added 542: , , F.Cu at (82.5, 87.6)
- added 543: , , F.Cu at (82.5, 85.1)
- added 544: , , F.Cu at (82.5, 82.5)
- added 545: , , F.Cu at (82.5, 80.0)
- added 546: , , F.Cu at (82.5, 77.5)
- added 547: , , F.Cu at (82.5, 74.9)
- added 548: , , F.Cu at (82.5, 72.4)
- added 549: , , F.Cu at (82.5, 69.8)
- added 550: , , F.Cu at (82.5, 67.3)
- added 551: , , F.Cu at (82.5, 64.8)
- added 552: , , F.Cu at (82.5, 62.2)
- added 553: , , F.Cu at (82.5, 59.7)
- added 554: , , F.Cu at (82.5, 57.1)
- added 555: , , F.Cu at (82.5, 54.6)
- added 556: , , F.Cu at (85.1, 146.1)
- added 557: , , F.Cu at (85.1, 143.5)
- added 558: , , F.Cu at (85.1, 141.0)
- added 559: , , F.Cu at (85.1, 138.4)
- added 560: , , F.Cu at (85.1, 135.9)
- added 561: , , F.Cu at (85.1, 133.3)
- added 562: , , F.Cu at (85.1, 130.8)
- added 563: , , F.Cu at (85.1, 128.3)
- added 564: , , F.Cu at (85.1, 125.7)
- added 565: , , F.Cu at (85.1, 123.2)
- added 566: , , F.Cu at (85.1, 120.7)
- added 567: , , F.Cu at (85.1, 118.1)
- added 568: , , F.Cu at (85.1, 115.6)
- added 569: , , F.Cu at (85.1, 113.0)
- added 570: , , F.Cu at (85.1, 110.5)
- added 571: , , F.Cu at (85.1, 108.0)
- added 572: , , F.Cu at (85.1, 105.4)
- added 573: , , F.Cu at (85.1, 102.9)
- added 574: , , F.Cu at (85.1, 100.3)
- added 575: , , F.Cu at (85.1, 97.8)
- added 576: , , F.Cu at (85.1, 95.2)
- added 577: , , F.Cu at (85.1, 92.7)
- added 578: , , F.Cu at (85.1, 90.2)
- added 579: , , F.Cu at (85.1, 87.6)
- added 580: , , F.Cu at (85.1, 85.1)
- added 581: , , F.Cu at (85.1, 82.5)
- added 582: , , F.Cu at (85.1, 80.0)
- added 583: , , F.Cu at (85.1, 77.5)
- added 584: , , F.Cu at (85.1, 74.9)
- added 585: , , F.Cu at (85.1, 72.4)
- added 586: , , F.Cu at (85.1, 69.8)
- added 587: , , F.Cu at (85.1, 67.3)
- added 588: , , F.Cu at (85.1, 64.8)
- added 589: , , F.Cu at (85.1, 62.2)
- added 590: , , F.Cu at (85.1, 59.7)
- added 591: , , F.Cu at (85.1, 57.1)
- added 592: , , F.Cu at (85.1, 54.6)
- added 593: , , F.Cu at (87.6, 146.1)
- added 594: , , F.Cu at (87.6, 143.5)
- added 595: , , F.Cu at (87.6, 141.0)
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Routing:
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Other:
- board text added: "sok"
- board text added: "wrp"
- board text removed: "gnd"
- board text removed: "sk"
- board text removed: "ww"

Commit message: update of 10x10 protoboards, conn connected
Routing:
- net (no net): track 4135.1 -> 4511.0 mm
